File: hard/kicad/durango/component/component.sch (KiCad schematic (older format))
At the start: 39 parts, among them J1 SCART, J2 Component Video [Pr/Pb/Y], Q1 BC548, Q2 BC548, Q3 BC548, Q4 BC548

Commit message: nanoLink board ready for ordering
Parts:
- added J3: Audio, durango:3xRCA, symbol Connector:Conn_Coaxial_x3
- C1, C2, C3, C4, C5, C6, C7, C8: footprint (none) -> Capacitor_THT:CP_Radial_D4.0mm_P1.50mm
- C10: value 100nF -> 22nF; footprint (none) -> Capacitor_THT:C_Rect_L7.0mm_W2.0mm_P5.00mm
- C9: footprint (none) -> Capacitor_THT:CP_Radial_D6.3mm_P2.50mm
- D1: footprint (none) -> LED_THT:LED_D3.0mm
- J1: footprint (none) -> durango:SCART
- J2: footprint (none) -> durango:3xRCA
- R1, R10, R11, R12, R13, R14, R15, R16, R17, R18, R19, R2, R20, R21, R22, R3, R4, R5, R6, R7, R8, R9: footprint (none) -> Resistor_THT:R_Axial_DIN0207_L6.3mm_D2.5mm_P10.16mm_Horizontal
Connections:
- net GND: now also J3.2 (GND1), J3.4 (GND2), J3.6 (GND3)
- net Y: now also J1.20 (Pin_20); no longer J1.19 (Pin_19)
- net AUDIO: now reaches J1.2 (Pin_2)
- net AUDIO: now also J1.6 (Pin_6), J3.1 (IN1), J3.3 (IN2)
- no-connect marks 7 -> 6

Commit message: almost definitive RGB to YUV converter
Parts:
- removed J3: Audio, durango:3xRCA, symbol Connector:Conn_Coaxial_x3
- added H1, H2, H3: M3, MountingHole:MountingHole_3.2mm_M3_DIN965, symbol Mechanical:MountingHole
- added J3: Audio, Connector_Phoenix_GMSTB:PhoenixContact_GMSTBA_2,5_3-G-7,62_1x03_P7.62mm_Horizontal, symbol Connector:Conn_Coaxial_x2
- added LOGO1: Logo_Open_Hardware_Small, durango:jaqueria, symbol Graphic:Logo_Open_Hardware_Small
- D1: value LED -> RGB mode
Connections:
- net AUDIO: now also J3.1 (IN1), J3.2 (IN2)
- net GND: now also J3.3 (EXT)
- no-connect marks 6 -> 5
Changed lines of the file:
@@
 P 1925 3975
 F 0 "D1" V 1925 4125 50  0000 R CNN
-F 1 "LED" V 1825 4125 50  0000 R CNN
+F 1 "RGB mode" V 1825 4125 50  0000 R CNN
 F 2 "LED_THT:LED_D3.0mm" H 1925 3975 50  0001 C CNN
 F 3 "~" H 1925 3975 50  0001 C CNN
@@
 Wire Wire Line
 	1700 3025 1700 4350
-$Comp
-L Connector:Conn_Coaxial_x3 J3
-U 1 1 64ABF1F2
-P 6125 4550
-F 0 "J3" H 6225 4553 50  0000 L CNN
-F 1 "Audio" H 6225 4462 50  0000 L CNN
-F 2 "durango:3xRCA" H 6125 4550 50  0001 C CNN
-F 3 " ~" H 6125 4550 50  0001 C CNN
-	1    6125 4550
-	1    0    0    -1
-$EndComp
 Wire Wire Line
 	5925 4550 5775 4550
@@
 Wire Wire Line
 	5775 4350 5925 4350
+Connection ~ 5875 3750
 Wire Wire Line
-	5875 4850 5875 4650
-Connection ~ 5875 3750
-Connection ~ 5875 4450
-Wire Wire Line
-	5875 4450 5875 3750
-Connection ~ 5875 4650
-Wire Wire Line
-	5875 4650 5875 4450
-NoConn ~ 5925 4750
+	5875 4750 5875 3750
 Text Label 5725 4350 2    50   ~ 0
 AUDIO
+$Comp
+L Connector:Conn_Coaxial_x2 J3
+U 1 1 64ADAA19
+P 6125 4450
+F 0 "J3" H 6225 4425 50  0000 L CNN
+F 1 "Audio" H 6225 4334 50  0000 L CNN
+F 2 "Connector_Phoenix_GMSTB:PhoenixContact_GMSTBA_2,5_3-G-7,62_1x03_P7.62mm_Horizontal" H 6125 4350 50  0001 C CNN
+F 3 " ~" H 6125 4350 50  0001 C CNN
+	1    6125 4450
+	1    0    0    -1
+$EndComp
+Wire Wire Line
+	6125 4750 5875 4750
+$Comp
+L Mechanical:MountingHole H1
+U 1 1 64B085AE
+P 3150 4775
+F 0 "H1" H 3250 4821 50  0000 L CNN
+F 1 "M3" H 3250 4730 50  0000 L CNN
+F 2 "MountingHole:MountingHole_3.2mm_M3_DIN965" H 3150 4775 50  0001 C CNN
+F 3 "~" H 3150 4775 50  0001 C CNN
+	1    3150 4775
+	1    0    0    -1
+$EndComp
+$Comp
+L Mechanical:MountingHole H2
+U 1 1 64B0D1E0
+P 3500 4775
+F 0 "H2" H 3600 4821 50  0000 L CNN
+F 1 "M3" H 3600 4730 50  0000 L CNN
+F 2 "MountingHole:MountingHole_3.2mm_M3_DIN965" H 3500 4775 50  0001 C CNN
+F 3 "~" H 3500 4775 50  0001 C CNN
+	1    3500 4775
+	1    0    0    -1
+$EndComp
+$Comp
+L Mechanical:MountingHole H3
+U 1 1 64B0DA00
+P 3875 4775
+F 0 "H3" H 3975 4821 50  0000 L CNN
+F 1 "M3" H 3975 4730 50  0000 L CNN
+F 2 "MountingHole:MountingHole_3.2mm_M3_DIN965" H 3875 4775 50  0001 C CNN
+F 3 "~" H 3875 4775 50  0001 C CNN
+	1    3875 4775
+	1    0    0    -1
+$EndComp
+$Comp
+L Graphic:Logo_Open_Hardware_Small LOGO1
+U 1 1 64B4A91C
+P 4675 4800
+F 0 "LOGO1" H 4675 5075 50  0001 C CNN
+F 1 "Logo_Open_Hardware_Small" H 4675 4575 50  0001 C CNN
+F 2 "durango:jaqueria" H 4675 4800 50  0001 C CNN
+F 3 "~" H 4675 4800 50  0001 C CNN
+	1    4675 4800
+	1    0    0    -1
+$EndComp
 $EndSCHEMATC

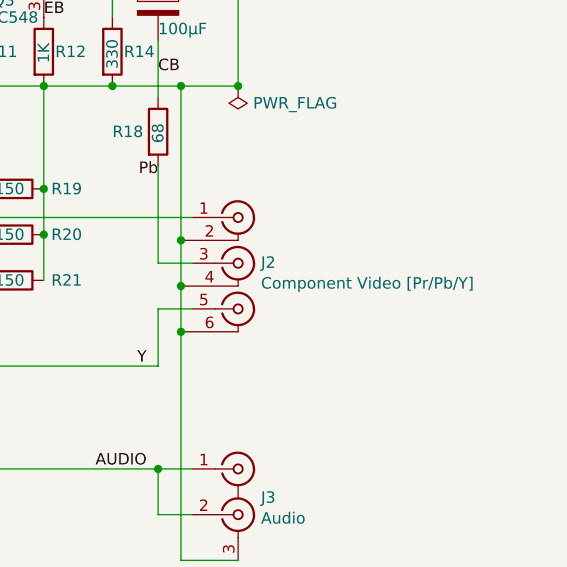
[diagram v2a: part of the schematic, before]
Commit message: put 2xRCA footprint on RGB2YUV
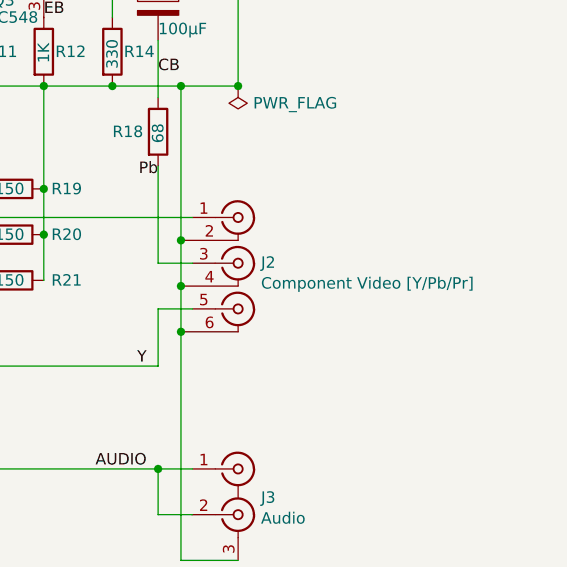
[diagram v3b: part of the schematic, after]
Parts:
- J2: value Component Video [Pr/Pb/Y] -> Component Video [Y/Pb/Pr]
- J3: footprint Connector_Phoenix_GMSTB:PhoenixContact_GMSTBA_2,5_3-G-7,62_1x03_P7.62mm_Horizontal -> durango:2xRCA_vertical
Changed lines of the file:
@@
 P 6125 3450
 F 0 "J2" H 6225 3453 50  0000 L CNN
-F 1 "Component Video [Pr/Pb/Y]" H 6225 3362 50  0000 L CNN
+F 1 "Component Video [Y/Pb/Pr]" H 6225 3362 50  0000 L CNN
 F 2 "durango:3xRCA" H 6125 3450 50  0001 C CNN
 F 3 " ~" H 6125 3450 50  0001 C CNN
@@
 F 0 "J3" H 6225 4425 50  0000 L CNN
 F 1 "Audio" H 6225 4334 50  0000 L CNN
-F 2 "Connector_Phoenix_GMSTB:PhoenixContact_GMSTBA_2,5_3-G-7,62_1x03_P7.62mm_Horizontal" H 6125 4350 50  0001 C CNN
+F 2 "durango:2xRCA_vertical" H 6125 4350 50  0001 C CNN
 F 3 " ~" H 6125 4350 50  0001 C CNN
 	1    6125 4450

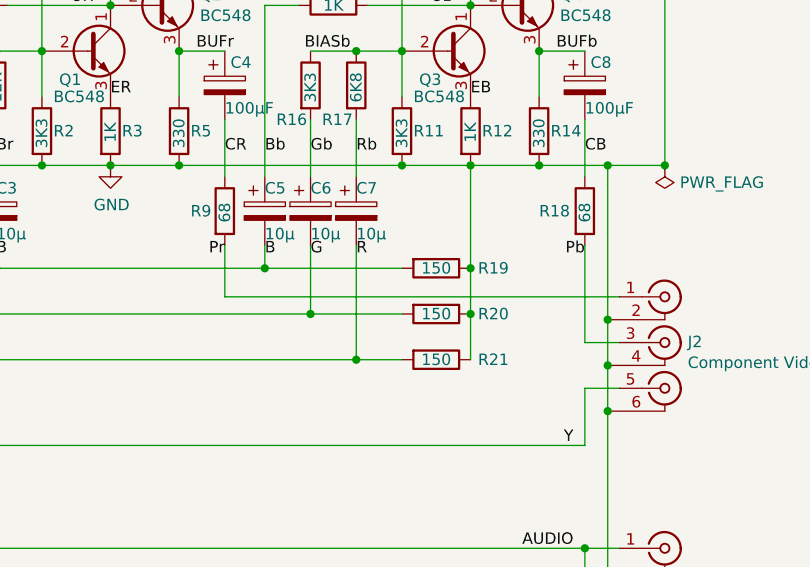
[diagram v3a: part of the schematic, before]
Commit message: revised RCA footprint and Component silkscreen
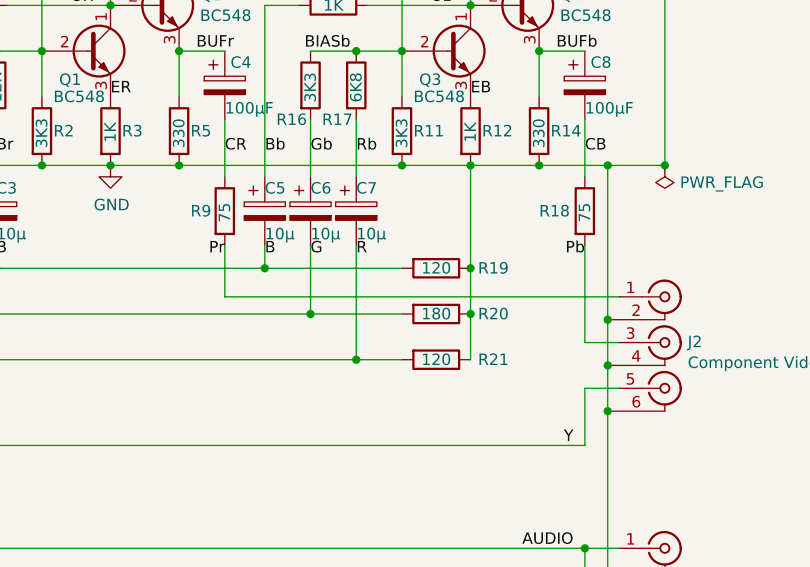
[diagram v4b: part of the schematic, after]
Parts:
- R18, R9: value 68 -> 75
- R19, R21: value 150 -> 120
- R20: value 150 -> 180
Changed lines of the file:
@@
 P 4200 2875
 F 0 "R9" H 4050 2875 50  0000 L CNN
-F 1 "68" V 4200 2825 50  0000 L CNN
+F 1 "75" V 4200 2825 50  0000 L CNN
 F 2 "Resistor_THT:R_Axial_DIN0207_L6.3mm_D2.5mm_P10.16mm_Horizontal" V 4130 2875 50  0001 C CNN
 F 3 "~" H 4200 2875 50  0001 C CNN
@@
 P 5775 2875
 F 0 "R18" H 5575 2875 50  0000 L CNN
-F 1 "68" V 5775 2825 50  0000 L CNN
+F 1 "75" V 5775 2825 50  0000 L CNN
 F 2 "Resistor_THT:R_Axial_DIN0207_L6.3mm_D2.5mm_P10.16mm_Horizontal" V 5705 2875 50  0001 C CNN
 F 3 "~" H 5775 2875 50  0001 C CNN
@@
 P 5125 3125
 F 0 "R19" V 5125 3375 50  0000 C CNN
-F 1 "150" V 5125 3125 50  0000 C CNN
+F 1 "120" V 5125 3125 50  0000 C CNN
 F 2 "Resistor_THT:R_Axial_DIN0207_L6.3mm_D2.5mm_P10.16mm_Horizontal" V 5055 3125 50  0001 C CNN
 F 3 "~" H 5125 3125 50  0001 C CNN
@@
 P 5125 3325
 F 0 "R20" V 5125 3575 50  0000 C CNN
-F 1 "150" V 5125 3325 50  0000 C CNN
+F 1 "180" V 5125 3325 50  0000 C CNN
 F 2 "Resistor_THT:R_Axial_DIN0207_L6.3mm_D2.5mm_P10.16mm_Horizontal" V 5055 3325 50  0001 C CNN
 F 3 "~" H 5125 3325 50  0001 C CNN
@@
 P 5125 3525
 F 0 "R21" V 5125 3775 50  0000 C CNN
-F 1 "150" V 5125 3525 50  0000 C CNN
+F 1 "120" V 5125 3525 50  0000 C CNN
 F 2 "Resistor_THT:R_Axial_DIN0207_L6.3mm_D2.5mm_P10.16mm_Horizontal" V 5055 3525 50  0001 C CNN
 F 3 "~" H 5125 3525 50  0001 C CNN
